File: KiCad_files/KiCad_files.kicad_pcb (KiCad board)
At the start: 2 copper layers, 80 x 100 mm, 73 parts, among them J1 Conn_01x02_Socket, J2 L717HDE15P, J3 Conn_01x03_Socket, SW1 WE430182070816, U1 LM22670QMR-5.0, U2 MC33275ST-3.3T3G, U3 ADM3488ExR, U6 LT1789

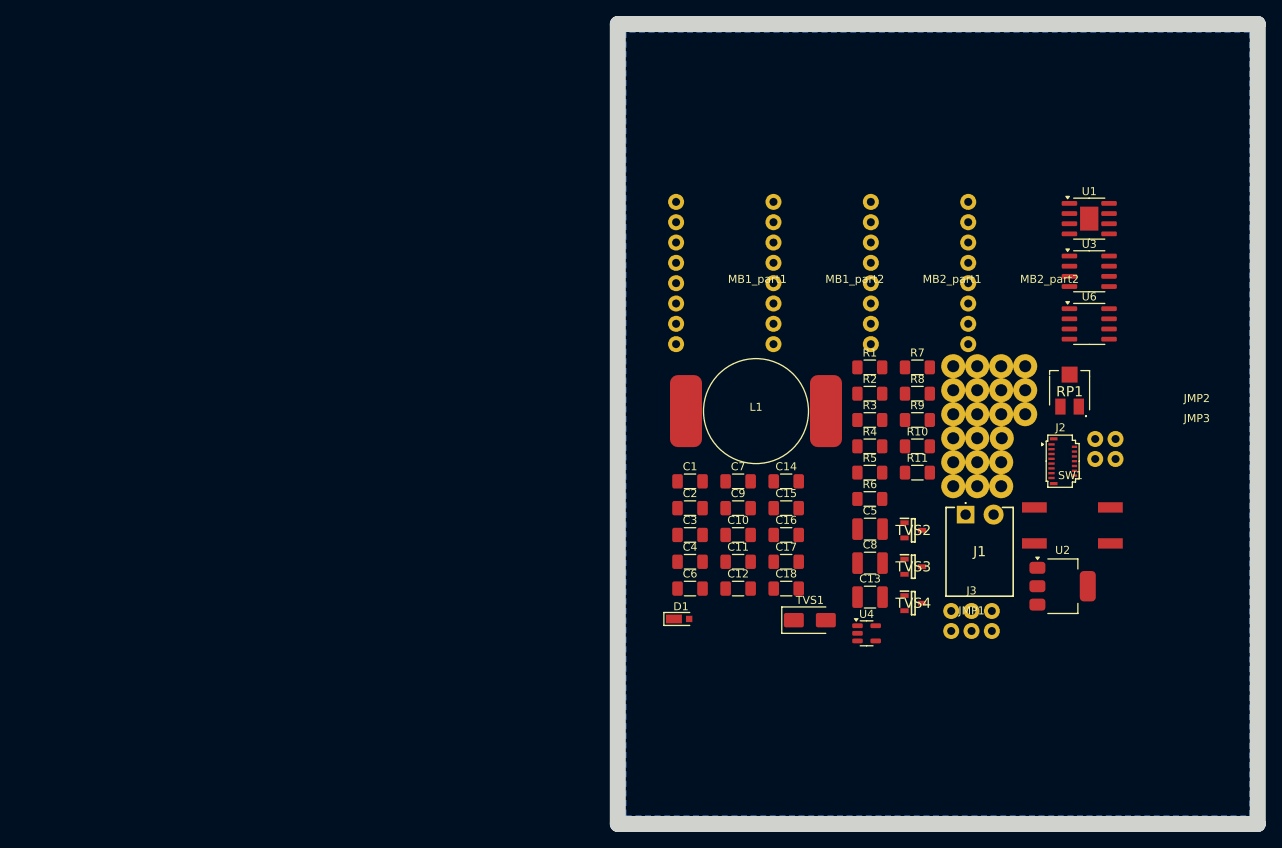
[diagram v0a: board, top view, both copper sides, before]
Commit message: Alligned microbus on PCB
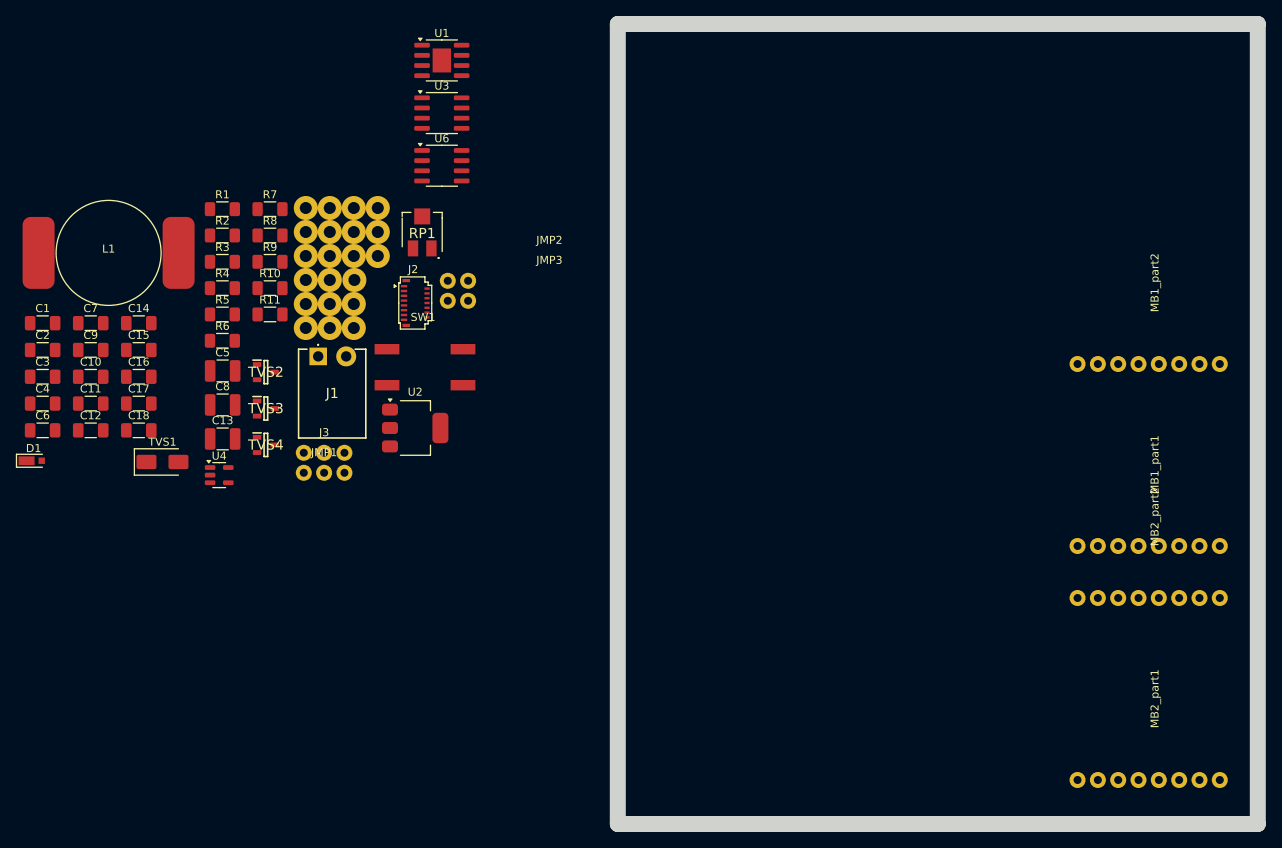
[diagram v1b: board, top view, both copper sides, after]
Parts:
- moved C10 83.3 mm to (34.1, 94.1)
- moved C11 83.3 mm to (34.1, 97.4)
- moved C12 83.3 mm to (34.1, 100.8)
- moved C13 83.3 mm to (50.6, 101.9)
- moved C5 83.3 mm to (50.6, 93.4)
- moved C7 83.3 mm to (34.1, 87.4)
- moved C8 83.3 mm to (50.6, 97.6)
- moved C9 83.3 mm to (34.1, 90.7)
- moved D1 83.3 mm to (27.0, 104.6)
- moved J2 83.3 mm to (74.7, 84.9)
- moved J3 83.3 mm to (63.3, 103.6)
- moved JMP1 83.3 mm to (63.3, 106.1)
- moved JMP2 83.3 mm to (78.8, 82.1)
- moved JMP3 83.3 mm to (78.8, 84.6)
- moved L1 83.3 mm to (36.4, 78.6)
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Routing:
- removed copper zone on B.Cu, net GNDA
